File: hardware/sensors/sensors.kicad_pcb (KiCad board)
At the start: 2 copper layers, 48 x 49 mm, 51 parts, among them J1 SWITCHES-SENSORS, J6 IRDA, SW1 SW_Push, SW2 SW_Push, SW3 SW_Push, SW4 SW_Push, U1 EKMC1604111, U2 DS18B20, U3 BME680, U4 BME280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

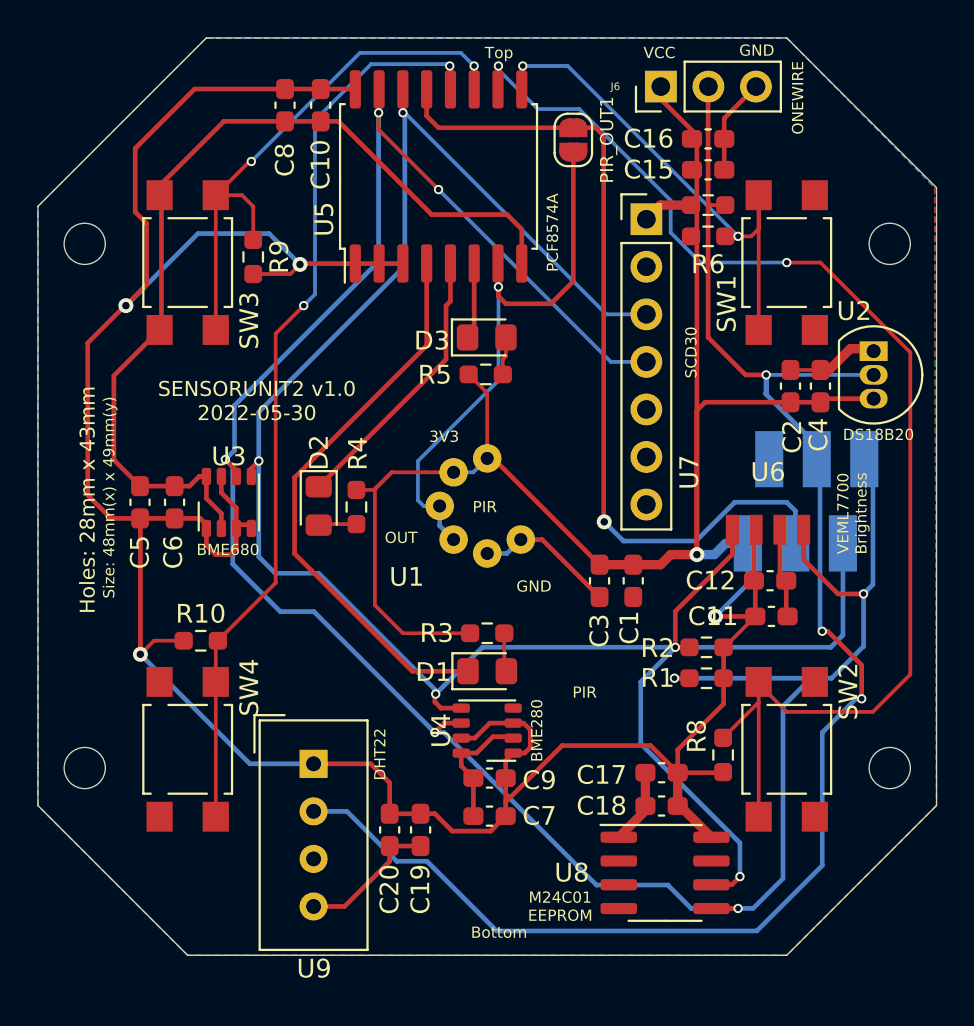
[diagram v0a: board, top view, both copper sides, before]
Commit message: feat: change PCB debug to EN/BOOT0
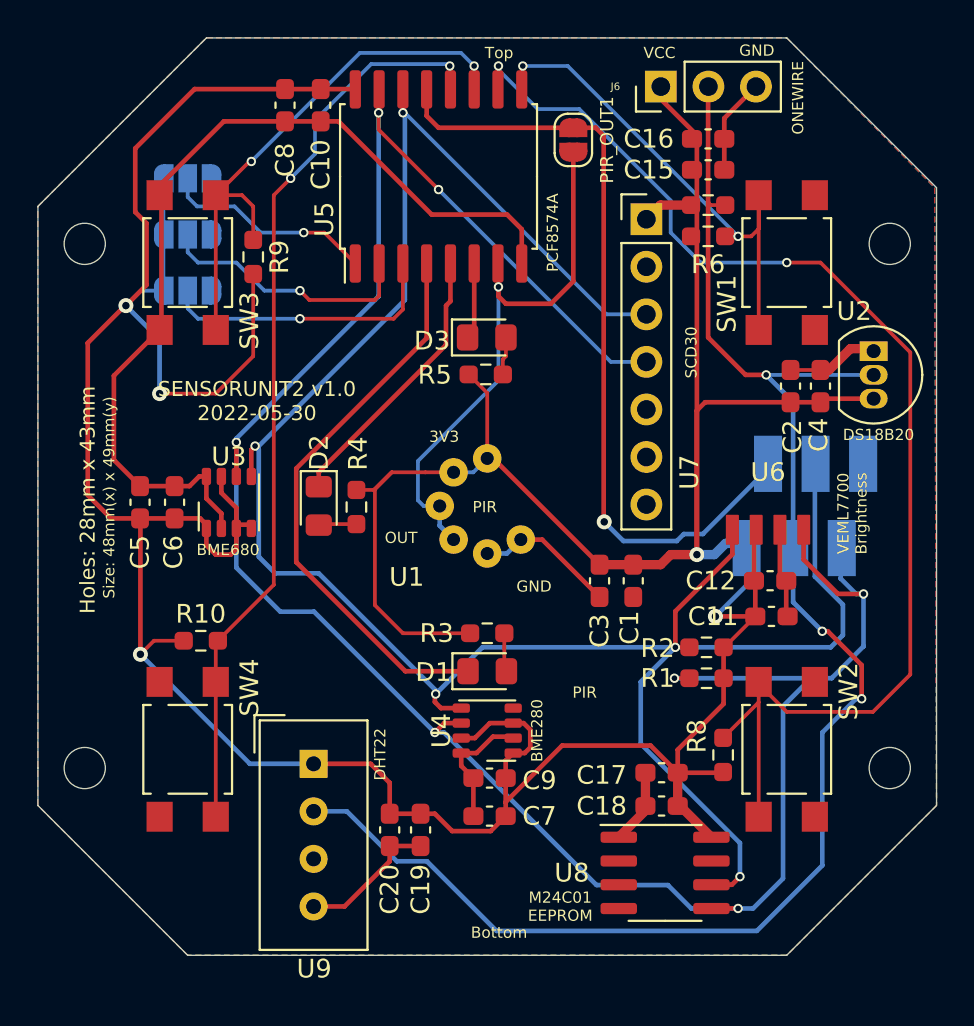
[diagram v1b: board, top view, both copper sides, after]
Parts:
- added A0: SolderJumper_3_Open, Jumper:SolderJumper-3_P1.3mm_Open_RoundedPad1.0x1.5mm, B.Cu at (87.0, 65.5)
- added A1: SolderJumper_3_Open, Jumper:SolderJumper-3_P1.3mm_Open_RoundedPad1.0x1.5mm, B.Cu at (87.0, 68.5)
- added A2: SolderJumper_3_Open, Jumper:SolderJumper-3_P1.3mm_Open_RoundedPad1.0x1.5mm, B.Cu at (87.0, 71.5)
- J1: value SWITCHES-SENSORS -> Button-Sensors-MicroMatch2X03
- moved J1 5.93 mm to (120.0, 83.0), turned to 90 degrees
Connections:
- J1 pad 1: +3V3 -> GND
- J1 pad 2: GND -> /SDA
- J1 pad 3: /OUT -> /SCL
- J1 pad 5: /SCL -> /OUT
- J1 pad 6: /SDA -> +3V3
- U5 pad 1: +3V3 -> /A0
- U5 pad 2: +3V3 -> /A1
- U5 pad 3: +3V3 -> /A2
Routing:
- net /A2: track 0.00 -> 15.3 mm, vias 0 -> 1
- net /A1: track 0.00 -> 14.0 mm, vias 0 -> 1
- net /A0: track 0.00 -> 11.4 mm, vias 0 -> 1
- net /SCL: track 114.6 -> 120.4 mm
- net /SDA: track 130.2 -> 126.0 mm
- net +3V3: track 239.5 -> 243.7 mm
- net /OUT: track 45.4 -> 43.0 mm
- net /ONEWIRE-IRDA: track 85.9 -> 84.8 mm
- net GND: track 89.8 -> 89.2 mm

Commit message: feat: Add fab export options for all pcbs
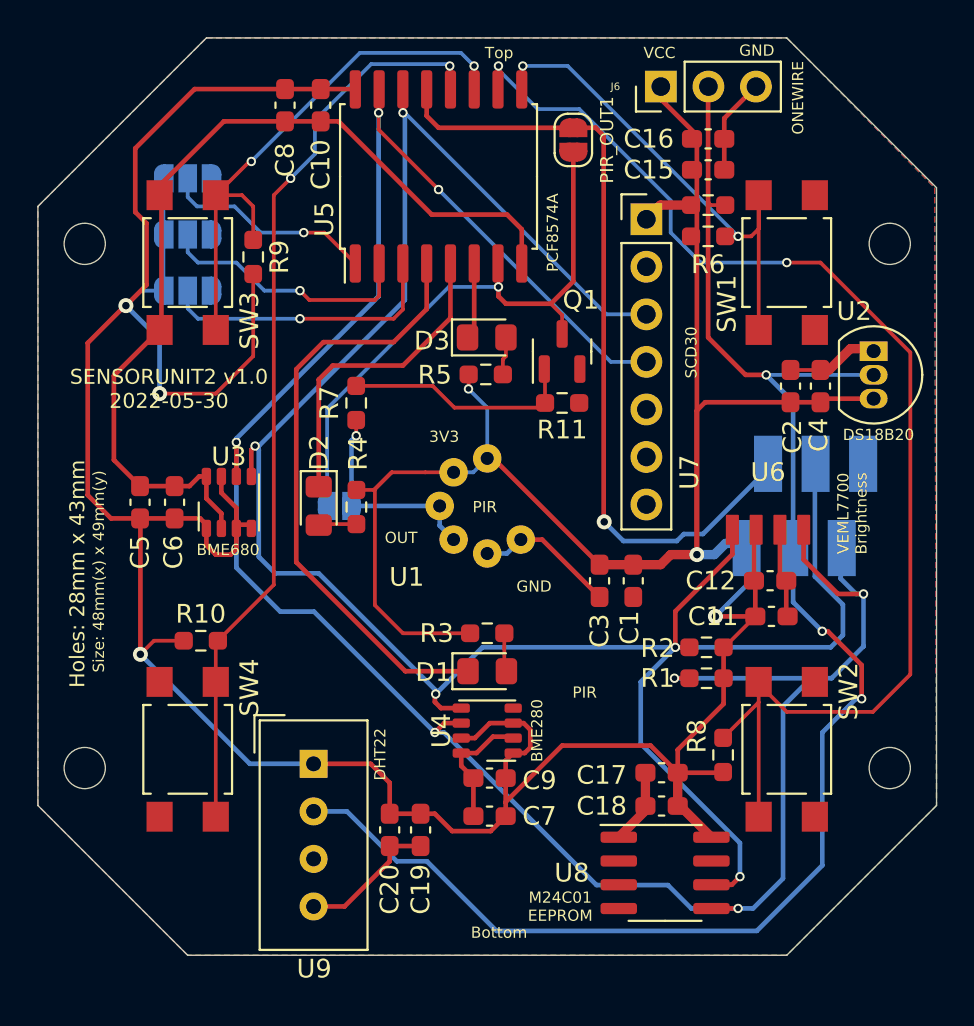
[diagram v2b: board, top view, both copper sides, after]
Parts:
- added Q1: BC849, Package_TO_SOT_SMD:SOT-23, F.Cu at (107.0, 74.8)
- added R11: 330R, Resistor_SMD:R_0603_1608Metric_Pad0.98x0.95mm_HandSolder, F.Cu at (107.0, 77.5)
- added R12: 0R, Jumper:SolderJumper-2_P1.3mm_Open_RoundedPad1.0x1.5mm, B.Cu at (95.1, 83.0)
- added R7: 10K, Resistor_SMD:R_0603_1608Metric_Pad0.98x0.95mm_HandSolder, F.Cu at (96.0, 77.5)
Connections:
- U1 pad 2: /PIR_OUT -> Net-(U1-Pad2)
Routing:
- net Net-(Q1-Pad1): track 0.00 -> 12.5 mm
- net Net-(U1-Pad2): track 0.00 -> 11.5 mm, vias 0 -> 1
- net /PIR_OUT: track 29.9 -> 32.2 mm
- net Net-(D1-Pad1): track 30.4 -> 32.6 mm
- net Net-(D2-Pad1): track 14.8 -> 17.0 mm
- net +3V3: vias 5 -> 6
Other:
- board text added: "PIR bypass"
